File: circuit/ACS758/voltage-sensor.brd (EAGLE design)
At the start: 40.6 x 40.6 mm, 7 parts, among them IC1 ACS758LCB-050B-PFF-T

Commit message: layout done
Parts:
- added U$3: COOBOC, hqc-logo:COOBOC
- moved R2 16.5 mm to (3.81, 17.8), turned to 270 degrees
- moved R3 14.0 mm to (10.1, 26.9)
- moved U$1 14.0 mm to (0.00, 24.1)
- moved U$2 14.0 mm to (40.6, 24.1)
- moved IC1 14.0 mm to (21.6, 26.7)
- moved JP1 14.0 mm to (36.8, 8.89)
- moved R1 10.5 mm to (7.62, 17.8), turned to 90 degrees
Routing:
- net VBAT: track 44.4 -> 33.1 mm, vias 2 -> 0
- net GND: track 43.4 -> 50.7 mm
- net V_VOL: track 37.0 -> 35.5 mm, vias 1 -> 0
- added copper zone on layer 1, net N$17
- added copper zone on layer 16, net N$18

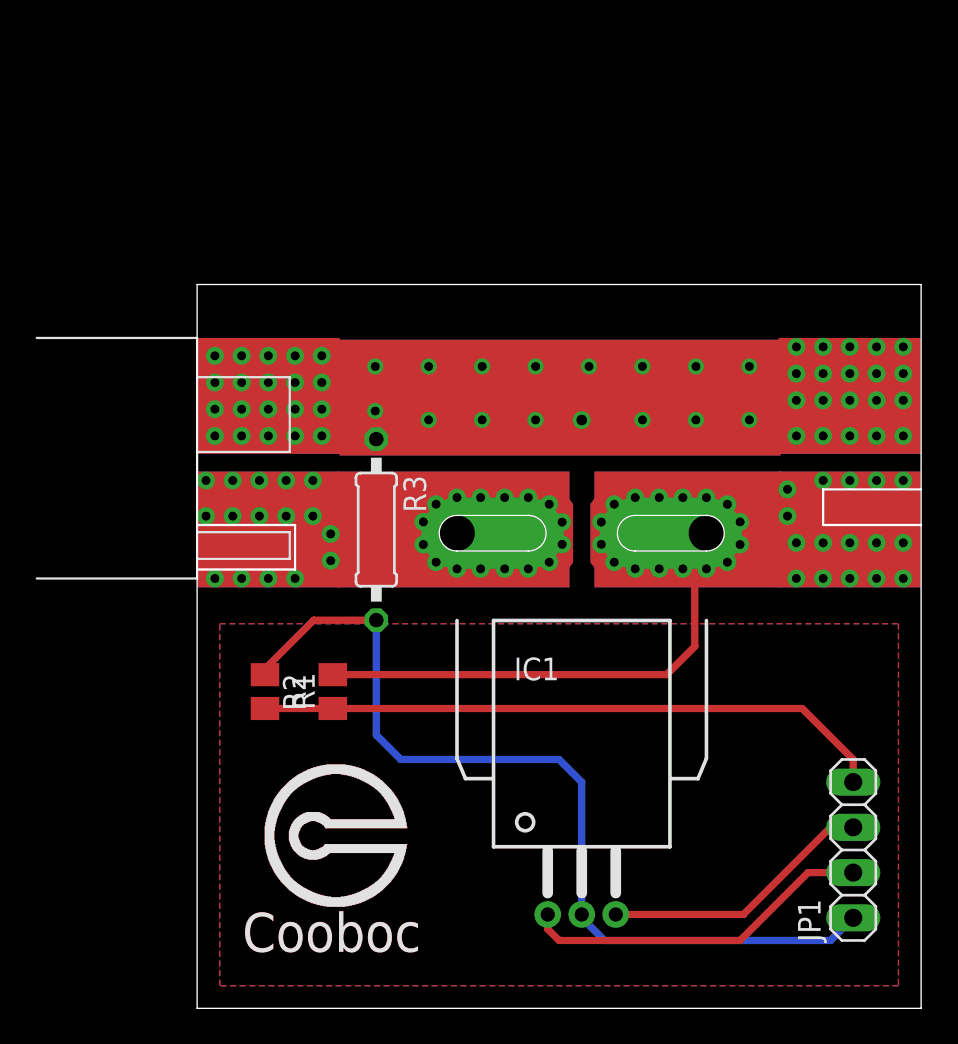
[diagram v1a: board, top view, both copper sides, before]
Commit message: add capicator on asc758
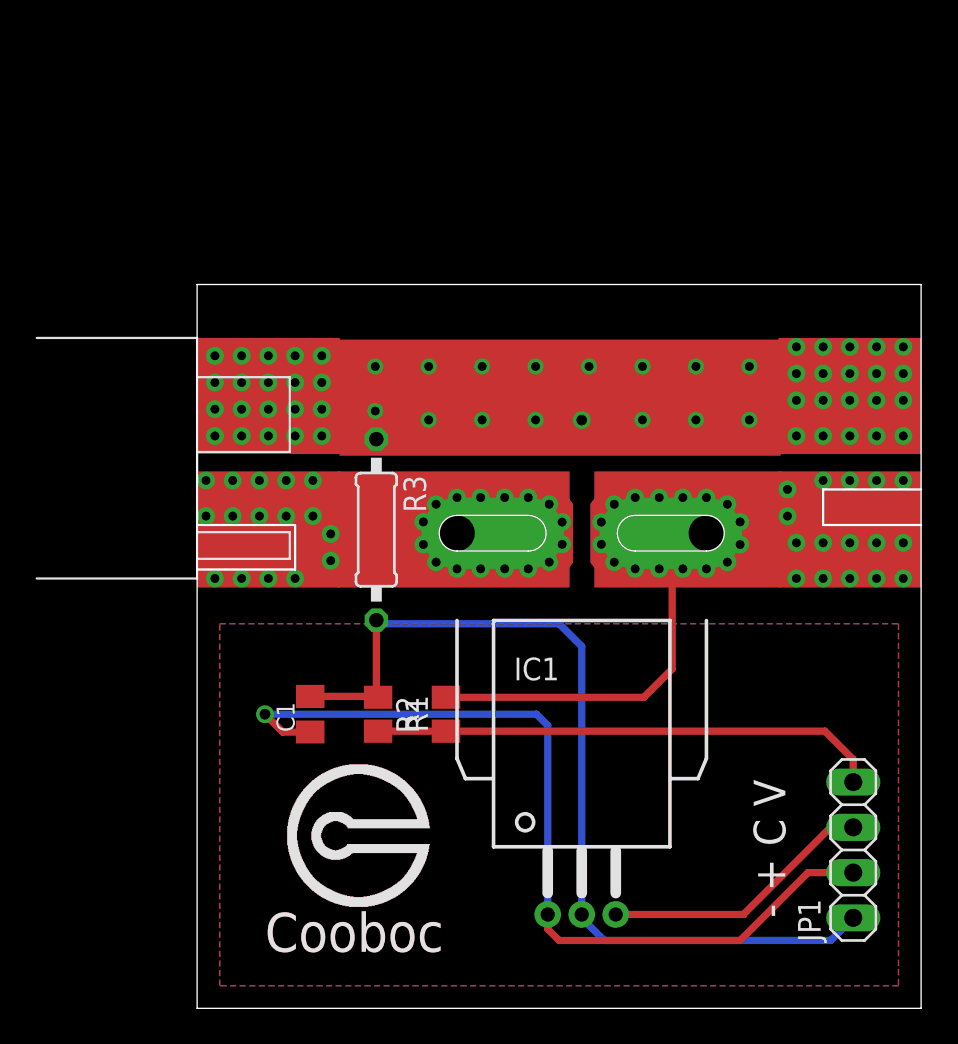
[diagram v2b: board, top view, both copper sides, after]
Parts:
- added C1: (no value), rcl:C0805K
- moved R1 6.48 mm to (14.0, 16.5)
- moved R2 6.48 mm to (10.2, 16.5)
- moved U$3 1.27 mm to (8.89, 7.62)
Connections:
- net GND: now also C1.2
- net VCC: now also C1.1
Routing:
- net VCC: track 19.8 -> 49.5 mm, vias 0 -> 1
- net V_VOL: track 35.5 -> 28.6 mm
- net VBAT: track 33.1 -> 29.3 mm
- net GND: track 50.7 -> 52.0 mm
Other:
- board text added: "- + C V"
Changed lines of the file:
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@@
 <layer number="29" name="tStop" color="7" fill="3" visible="yes" active="yes"/>
 <layer number="30" name="bStop" color="7" fill="6" visible="yes" active="yes"/>
-<layer number="31" name="tCream" color="7" fill="4" visible="no" active="yes"/>
-<layer number="32" name="bCream" color="7" fill="5" visible="no" active="yes"/>
-<layer number="33" name="tFinish" color="6" fill="3" visible="no" active="yes"/>
-<layer number="34" name="bFinish" color="6" fill="6" visible="no" active="yes"/>
-<layer number="35" name="tGlue" color="7" fill="4" visible="no" active="yes"/>
-<layer number="36" name="bGlue" color="7" fill="5" visible="no" active="yes"/>
-<layer number="37" name="tTest" color="7" fill="1" visible="no" active="yes"/>
-<layer number="38" name="bTest" color="7" fill="1" visible="no" active="yes"/>
+<layer number="31" name="tCream" color="7" fill="4" visible="yes" active="yes"/>
+<layer number="32" name="bCream" color="7" fill="5" visible="yes" active="yes"/>
+<layer number="33" name="tFinish" color="6" fill="3" visible="yes" active="yes"/>
+<layer number="34" name="bFinish" color="6" fill="6" visible="yes" active="yes"/>
+<layer number="35" name="tGlue" color="7" fill="4" visible="yes" active="yes"/>
+<layer number="36" name="bGlue" color="7" fill="5" visible="yes" active="yes"/>
+<layer number="37" name="tTest" color="7" fill="1" visible="yes" active="yes"/>
+<layer number="38" name="bTest" color="7" fill="1" visible="yes" active="yes"/>
 <layer number="39" name="tKeepout" color="4" fill="11" visible="yes" active="yes"/>
 <layer number="40" name="bKeepout" color="1" fill="11" visible="yes" active="yes"/>
@@
 <layer number="42" name="bRestrict" color="1" fill="10" visible="yes" active="yes"/>
 <layer number="43" name="vRestrict" color="2" fill="10" visible="yes" active="yes"/>
-<layer number="44" name="Drills" color="7" fill="1" visible="no" active="yes"/>
-<layer number="45" name="Holes" color="7" fill="1" visible="no" active="yes"/>
+<layer number="44" name="Drills" color="7" fill="1" visible="yes" active="yes"/>
+<layer number="45" name="Holes" color="7" fill="1" visible="yes" active="yes"/>
 <layer number="46" name="Milling" color="3" fill="1" visible="yes" active="yes"/>
-<layer number="47" name="Measures" color="7" fill="1" visible="no" active="yes"/>
+<layer number="47" name="Measures" color="7" fill="1" visible="yes" active="yes"/>
 <layer number="48" name="Document" color="7" fill="1" visible="yes" active="yes"/>
 <layer number="49" name="Reference" color="7" fill="1" visible="yes" active="yes"/>
@@
 <rectangle x1="22.3" y1="23.63" x2="32.6" y2="30.13" layer="30"/>
 <rectangle x1="22.3" y1="23.63" x2="32.7" y2="30.13" layer="29"/>
+<text x="33.02" y="5.08" size="1.778" layer="25" rot="R90">- + C V</text>
 </plain>
 <attributes>
@@
 <element name="U$1" library="connector" package="T-FEMALE" value="T-PLUG-FEMALE" x="0" y="24.13"/>
 <element name="U$2" library="connector" package="T-MALE" value="T-PLUG-MALE" x="40.64" y="24.13" rot="MR0"/>
-<element name="R1" library="resistor" package="M0805" value="" x="7.62" y="17.78" rot="R90"/>
-<element name="R2" library="resistor" package="M0805" value="" x="3.81" y="17.78" rot="R270"/>
+<element name="R1" library="resistor" package="M0805" value="" x="13.97" y="16.51" rot="R90"/>
+<element name="R2" library="resistor" package="M0805" value="" x="10.16" y="16.51" rot="R270"/>
 <element name="R3" library="resistor" package="0207/10" value="" x="10.06" y="26.87" rot="R270"/>
-<element name="U$3" library="hqc-logo" package="COOBOC" value="COOBOC" x="7.62" y="7.62"/>
+<element name="U$3" library="hqc-logo" package="COOBOC" value="COOBOC" x="8.89" y="7.62"/>
+<element name="C1" library="rcl" package="C0805K" value="" x="6.35" y="16.51" rot="R90"/>
 </elements>
 <signals>
@@
 <wire x1="22.86" y1="3.81" x2="35.56" y2="3.81" width="0.4064" layer="16"/>
 <wire x1="35.56" y1="3.81" x2="36.83" y2="5.08" width="0.4064" layer="16"/>
-<wire x1="10.06" y1="21.79" x2="6.55" y2="21.79" width="0.4064" layer="1"/>
-<wire x1="6.55" y1="21.79" x2="3.81" y2="19.05" width="0.4064" layer="1"/>
-<wire x1="3.81" y1="19.05" x2="3.81" y2="18.73" width="0.4064" layer="1"/>
-<wire x1="10.06" y1="21.79" x2="10.06" y2="15.34" width="0.4064" layer="16"/>
-<wire x1="10.06" y1="15.34" x2="11.43" y2="13.97" width="0.4064" layer="16"/>
-<wire x1="11.43" y1="13.97" x2="20.32" y2="13.97" width="0.4064" layer="16"/>
-<wire x1="20.32" y1="13.97" x2="21.59" y2="12.7" width="0.4064" layer="16"/>
-<wire x1="21.59" y1="12.7" x2="21.59" y2="5.27" width="0.4064" layer="16"/>
+<contactref element="C1" pad="2"/>
+<wire x1="6.35" y1="17.51" x2="10.16" y2="17.51" width="0.4064" layer="1"/>
+<wire x1="10.16" y1="17.51" x2="10.16" y2="17.46" width="0.4064" layer="1"/>
+<wire x1="10.16" y1="17.46" x2="10.06" y2="17.46" width="0.4064" layer="1"/>
+<wire x1="10.06" y1="17.46" x2="10.06" y2="21.79" width="0.4064" layer="1"/>
+<wire x1="21.59" y1="5.27" x2="21.59" y2="20.32" width="0.4064" layer="16"/>
+<wire x1="21.59" y1="20.32" x2="20.32" y2="21.59" width="0.4064" layer="16"/>
+<wire x1="20.32" y1="21.59" x2="10.26" y2="21.59" width="0.4064" layer="16"/>
+<wire x1="10.26" y1="21.59" x2="10.06" y2="21.79" width="0.4064" layer="16"/>
 </signal>
 <signal name="VBAT">
@@
 <contactref element="IC1" pad="IP+@17" route="any" routetag="G$1.IP+"/>
 <contactref element="R1" pad="2"/>
-<wire x1="7.62" y1="18.73" x2="26.35" y2="18.73" width="0.4064" layer="1"/>
-<wire x1="26.35" y1="18.73" x2="27.94" y2="20.32" width="0.4064" layer="1"/>
-<wire x1="27.94" y1="20.32" x2="27.94" y2="24.02" width="0.4064" layer="1"/>
-<wire x1="27.94" y1="24.02" x2="28.59" y2="24.67" width="0.4064" layer="1"/>
 <wire x1="30.48" y1="27.305" x2="36.815" y2="27.305" width="0.4064" layer="16"/>
 <wire x1="36.815" y1="27.305" x2="37.64" y2="28.13" width="0.4064" layer="16"/>
+<wire x1="13.97" y1="17.46" x2="25.08" y2="17.46" width="0.4064" layer="1"/>
+<wire x1="25.08" y1="17.46" x2="26.67" y2="19.05" width="0.4064" layer="1"/>
+<wire x1="26.67" y1="19.05" x2="26.67" y2="24.75" width="0.4064" layer="1"/>
+<wire x1="26.67" y1="24.75" x2="28.59" y2="26.67" width="0.4064" layer="1"/>
 </signal>
 <signal name="V_VOL">
@@
 <contactref element="R1" pad="1"/>
 <contactref element="R2" pad="2"/>
-<wire x1="3.81" y1="16.83" x2="7.62" y2="16.83" width="0.4064" layer="1"/>
-<wire x1="7.62" y1="16.83" x2="33.97" y2="16.83" width="0.4064" layer="1"/>
-<wire x1="33.97" y1="16.83" x2="36.83" y2="13.97" width="0.4064" layer="1"/>
+<wire x1="10.16" y1="15.56" x2="13.97" y2="15.56" width="0.4064" layer="1"/>
+<wire x1="13.97" y1="15.56" x2="35.24" y2="15.56" width="0.4064" layer="1"/>
+<wire x1="35.24" y1="15.56" x2="36.83" y2="13.97" width="0.4064" layer="1"/>
 <wire x1="36.83" y1="13.97" x2="36.83" y2="12.7" width="0.4064" layer="1"/>
 </signal>
@@
 <wire x1="30.48" y1="3.81" x2="34.29" y2="7.62" width="0.4064" layer="1"/>
 <wire x1="34.29" y1="7.62" x2="36.83" y2="7.62" width="0.4064" layer="1"/>
+<contactref element="C1" pad="1"/>
+<wire x1="6.35" y1="15.51" x2="4.81" y2="15.51" width="0.4064" layer="1"/>
+<wire x1="19.68" y1="5.27" x2="19.68" y2="15.88" width="0.4064" layer="16"/>
+<wire x1="19.68" y1="15.88" x2="19.05" y2="16.51" width="0.4064" layer="16"/>
+<wire x1="19.05" y1="16.51" x2="3.81" y2="16.51" width="0.4064" layer="16"/>
+<via x="3.81" y="16.51" extent="1-16" drill="0.6"/>
+<wire x1="3.81" y1="16.51" x2="4.81" y2="15.51" width="0.4064" layer="1"/>
 </signal>
 <signal name="V_CUR">
